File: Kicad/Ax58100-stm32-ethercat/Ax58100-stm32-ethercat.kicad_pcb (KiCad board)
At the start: 2 copper layers, 94.5 x 74.4 mm, 184 parts, among them J1 Step1, J10 Encoder, J11 5V Power IN, J12 24V Field, J13 DAC, J14 In_opt1, J15 Serial usart1, J16 In_opt2, J17 STLINK, J18 Out_opt, J2 Step2, J3 Step3, J4 Step4, J5 THCAD, J6 In1-4, J7 In5-8, J8 Output1-2, J9 Output3-4, SW1 SW PB, U1 MAX3485CSA/ESA, U10 AX58100, U2 TXS0108EPW, U3 TLP292-4, U4 TLP292-4, U5 TLP292-4, U6 STM32F407VGT6, U7 AMS1117-3.3, U8 24LC32A, U9 AMS1117-1.2, Y1 8 MHz, Y2 NXK25.000AE12F-KAB6-12

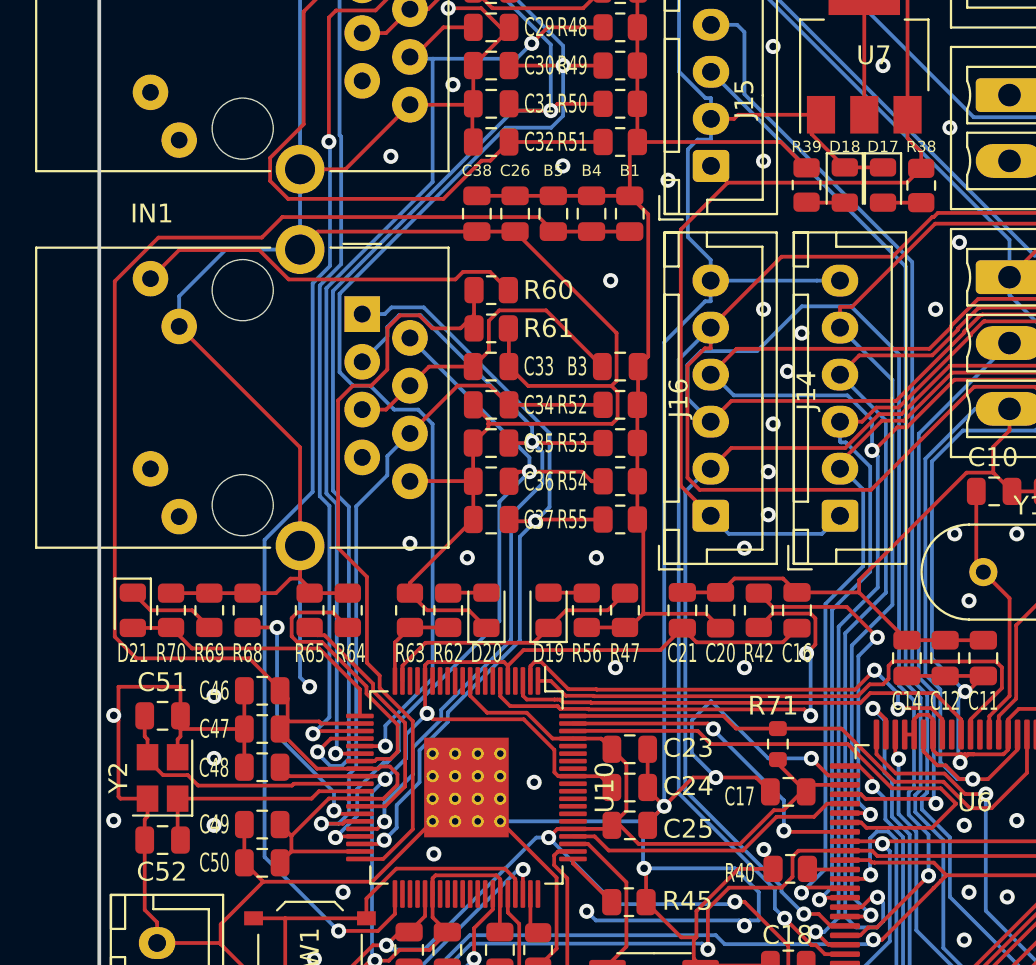
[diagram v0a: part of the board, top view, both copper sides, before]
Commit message: all leds are now 0603
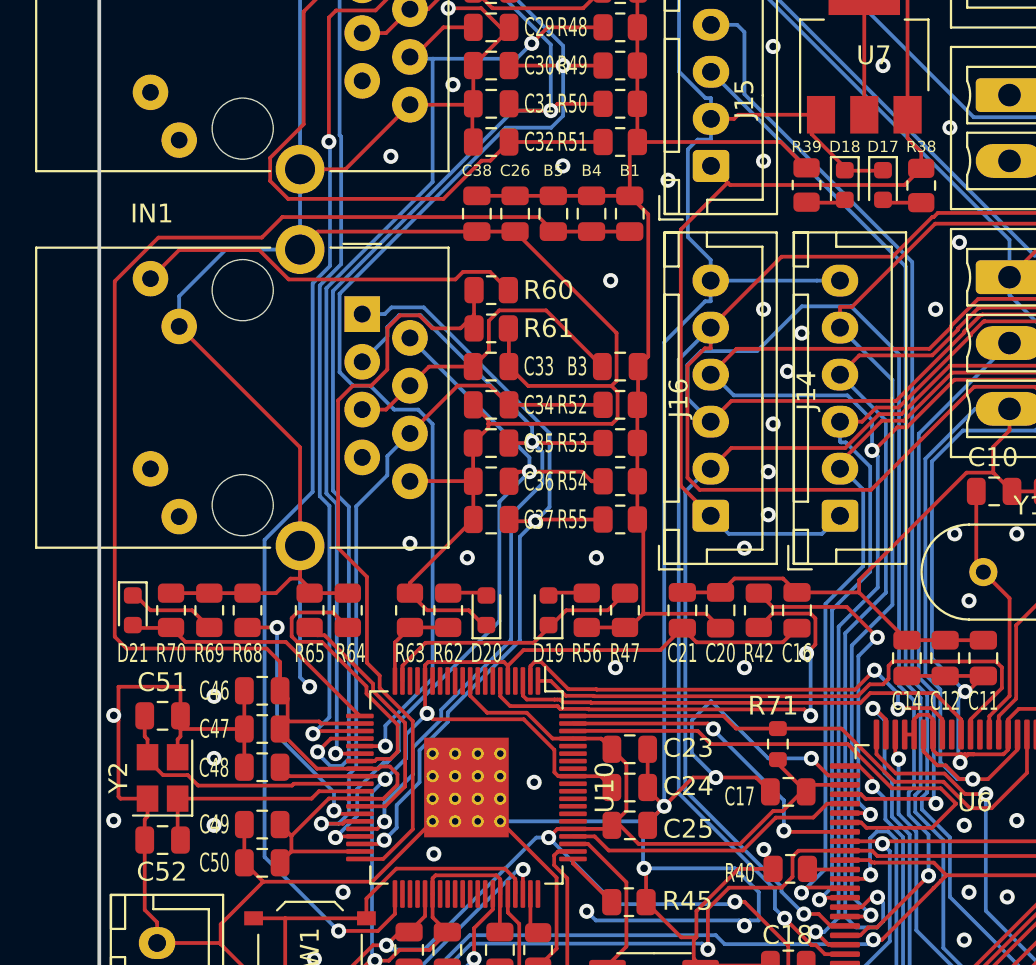
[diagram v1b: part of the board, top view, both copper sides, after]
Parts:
- D17, D18, D19, D20, D21: footprint LED_SMD:LED_0805_2012Metric -> LED_SMD:LED_0603_1608Metric
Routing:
- net +3.3VA: track 85.0 -> 85.8 mm
- net EEP_DONE: track 14.8 -> 14.0 mm

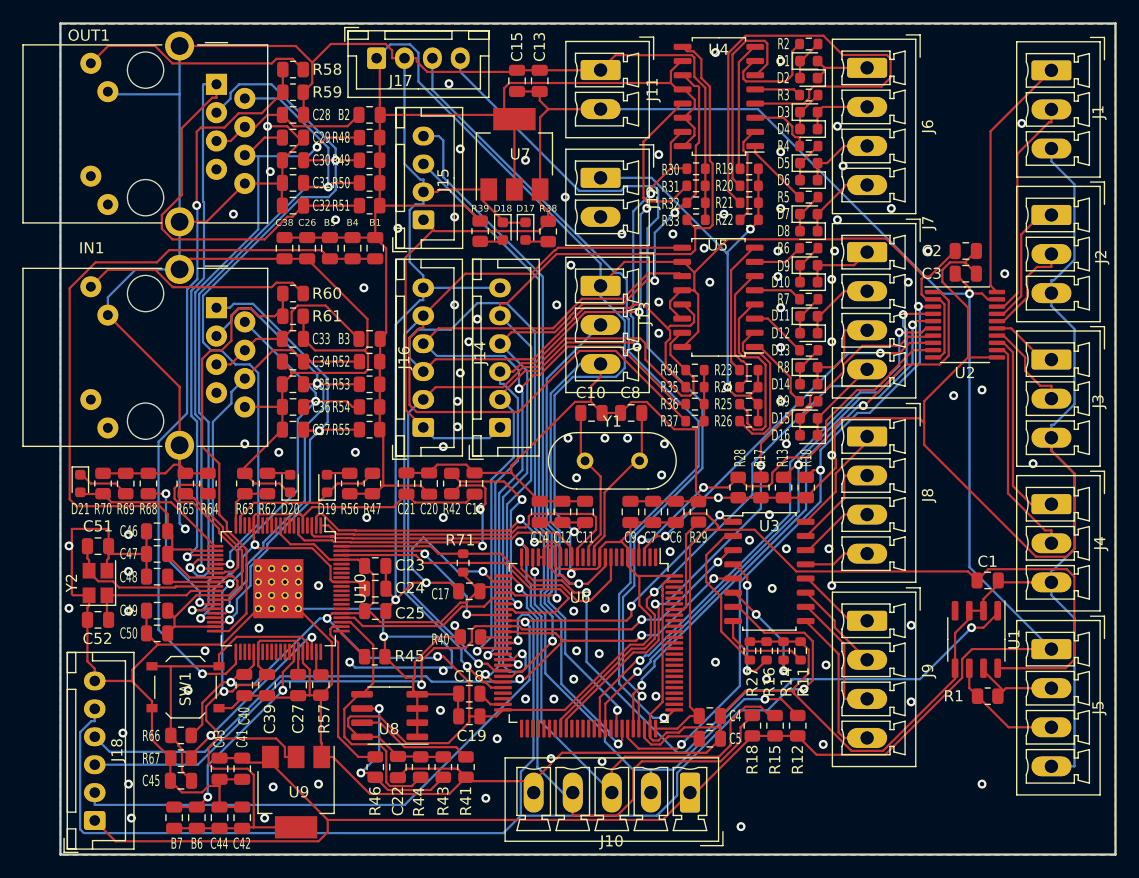
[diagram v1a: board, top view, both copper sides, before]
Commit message: morfe copper in +5V leads
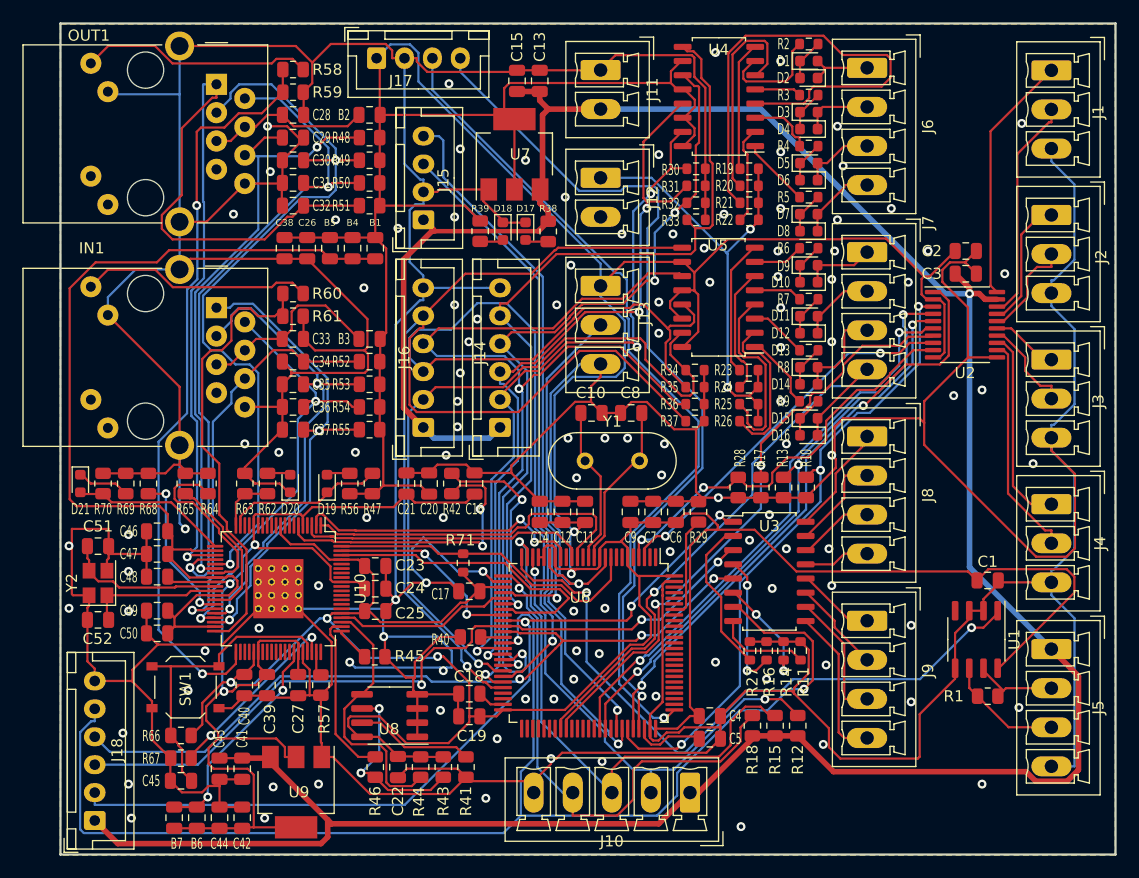
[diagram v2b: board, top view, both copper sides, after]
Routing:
- net +5V: track 245.6 -> 258.4 mm
- net GND: track 825.9 -> 829.7 mm
- net +3.3V: track 457.7 -> 454.2 mm

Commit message: Getting ready for fab
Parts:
- renumbered R71 to R42, R42 to R43, R43 to R44, R44 to R45, R45 to R46, R46 to R47, R47 to R48, R48 to R49, R49 to R50, R50 to R51, R51 to R52, R52 to R53, R53 to R54, R54 to R55, R55 to R56, R56 to R57, R57 to R58, R58 to R59, R59 to R60, R60 to R61, R61 to R62, R62 to R63, R63 to R64, R64 to R65, R65 to R66, R66 to R67, R67 to R68, R68 to R69, R69 to R70, R70 to R71
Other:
- board text added: "- + 24V"
- board text added: "1 2 3 4 IN"
- board text added: "1+ 1- 2+ 2- OUT"
- board text added: "2- 2+ 1- 1+ OUT"
- board text added: "3+ 3- 4+ 4- OUT"
- board text added: "4 3 2 1 IN"
- board text added: "4- 4+ 3- 3+ OUT"
- board text added: "5 6 7 8 IN"
- board text added: "8 5 IN"
- board text added: "DAC"
- board text added: "EaserCAT 3000 by MetalMusings"
- board text added: "EaserCAT 3000 by MetalMusings Feb 2024 v1"
- board text added: "Encoder"
- board text added: "GND +5V"
- board text added: "IN"
- board text added: "OUT"
- board text added: "Step 1"
- board text added: "Step 2"
- board text added: "Step 3"
- board text added: "Step 4"
- board text added: "THCAD"
